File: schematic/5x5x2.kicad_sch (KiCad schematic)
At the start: 158 parts, among them J1 SW Debug, SW11 SW, SW12 SW, SW13 SW, SW14 SW, SW15 SW, SW21 SW, SW22 SW, SW23 SW, SW24 SW, SW25 SW, SW31 SW, SW41 SW, SW42 SW, SW43 SW, SW44 SW, SW45 SW, SW51 SW, SW52 SW, SW53 SW, SW54 SW, SW55 SW

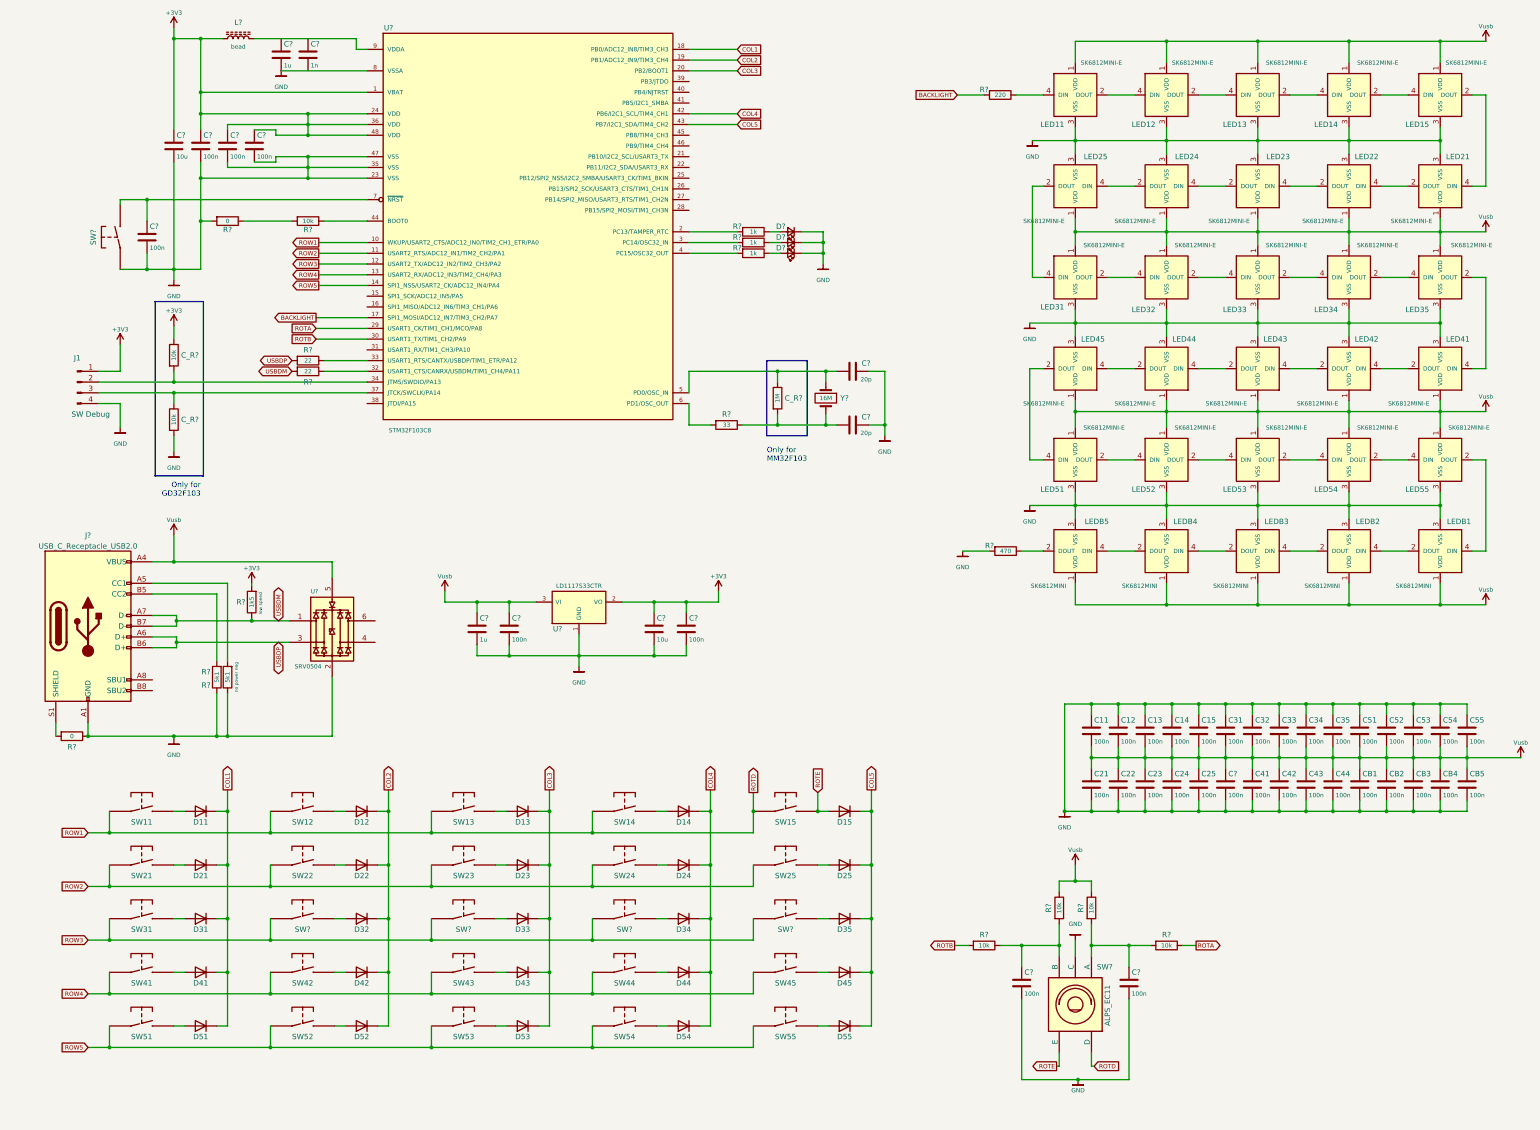
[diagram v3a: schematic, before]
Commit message: Started assigning footprints
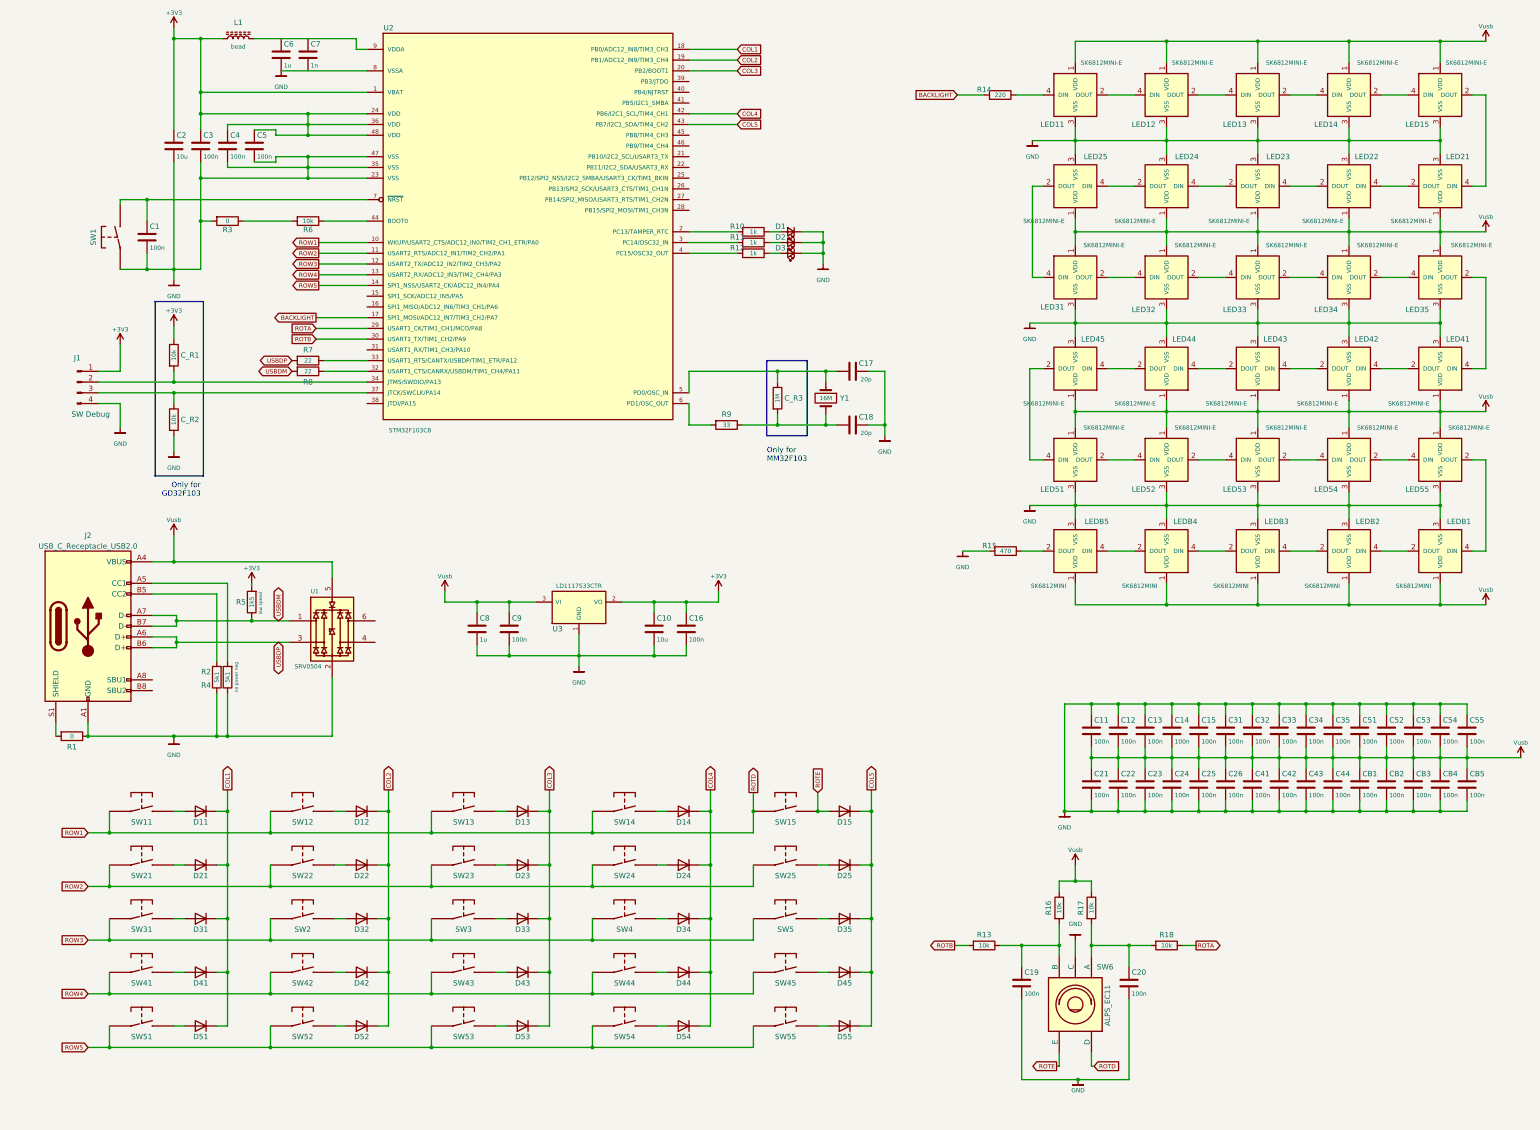
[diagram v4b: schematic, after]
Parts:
- gave numbers to parts that had none: 52

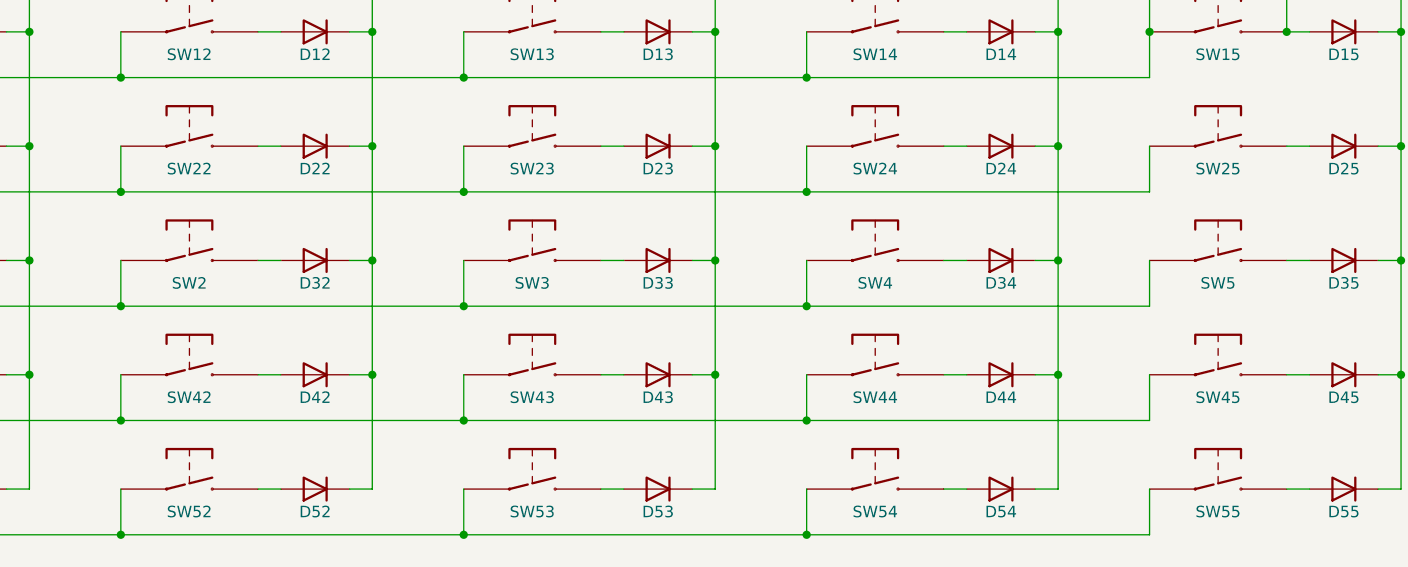
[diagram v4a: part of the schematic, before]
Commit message: Added footprints, started pcb
- used easyeda converter to get lcsc parts
- used the kicad standard addon kbd library for the kailh socket
- used foostans sk6812
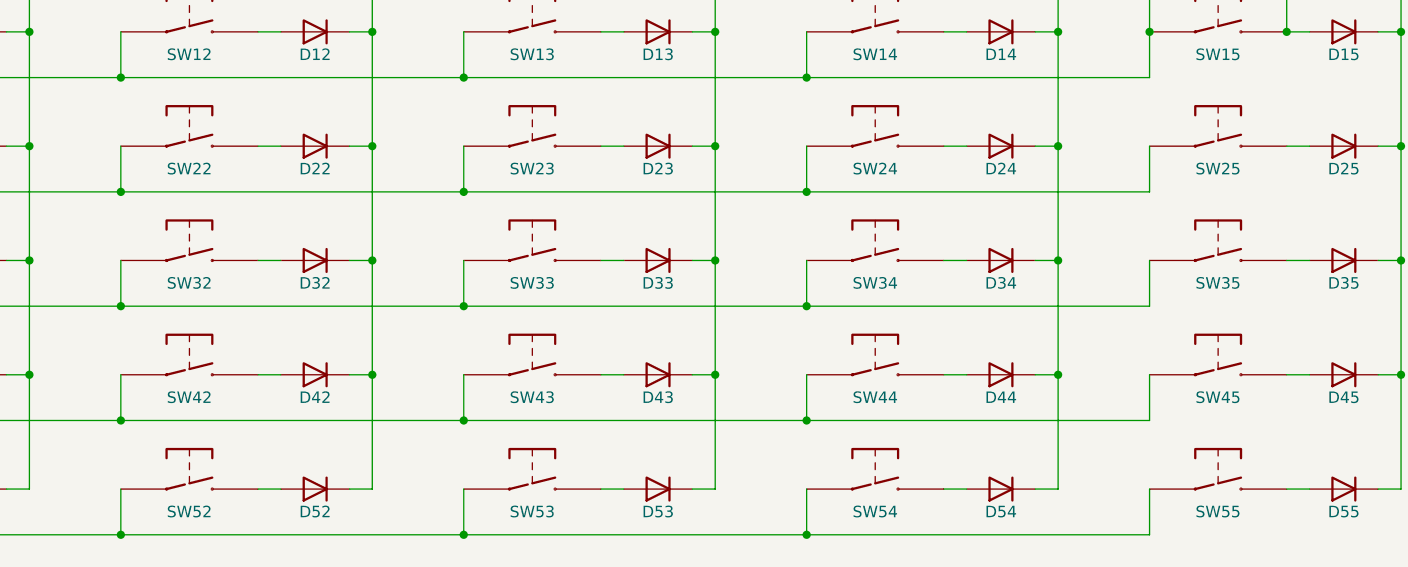
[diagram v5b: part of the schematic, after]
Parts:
- C1, C10, C19, C2, C20, C6, C7, C8: footprint Capacitors_SMD:C_1206 -> (none)
- C11, C12, C13, C14, C15, C16, C17, C18, C21, C22, C23, C24, C25, C26, C3, C31, C32, C33, C34, C35, C4, C41, C42, C43, C44, C5, C51, C52, C53, C54, C55, C9, CB1, CB2, CB3, CB4, CB5, L1: footprint Capacitors_SMD:C_0805 -> (none)
- C_R1, C_R2, C_R3, R1, R10, R11, R12, R13, R14, R15, R16, R17, R18, R2, R3, R4, R5, R6, R7, R8, R9: footprint Resistors_SMD:R_0805 -> (none)
- D1, D2, D3: footprint LEDs:LED-0805 -> (none)
- D11, D12, D13, D14, D15, D21, D22, D23, D24, D25, D31, D32, D33, D34, D35, D41, D42, D43, D44, D45, D51, D52, D53, D54, D55: footprint Diodes_ThroughHole:Diode_DO-35_SOD27_Horizontal_RM10 -> Diode_SMD:D_SOD-123F
- J1: footprint (none) -> Connector_PinSocket_2.54mm:PinSocket_1x04_P2.54mm_Vertical
- LED11: footprint SK68xx:SK6812MINI-E -> (none)
- LED12, LED13, LED14, LED15, LED21, LED22, LED23, LED24, LED25, LED31, LED32, LED33, LED34, LED35, LED41, LED42, LED43, LED44, LED45, LED51, LED52, LED53, LED54, LED55: footprint kbd:YS-SK6812MINI-E -> (none)
- LEDB1, LEDB2, LEDB3, LEDB4, LEDB5: footprint SK68xx:SK6812MINI -> (none)
- SW1: footprint WD_Packages:CHERRY_PCB_DG2 -> (none)
- renumbered SW2 to SW32, SW3 to SW33, SW4 to SW34, SW5 to SW35
